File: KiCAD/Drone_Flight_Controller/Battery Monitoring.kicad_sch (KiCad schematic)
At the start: 7 parts, among them U2 AS358

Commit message: Add Components to BOM
Add Components to BOM
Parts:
- added unit 1 of U2
- R11, R15: footprint (none) -> Resistor_SMD:R_0805_2012Metric_Pad1.20x1.40mm_HandSolder; Link (none) -> https://www.mouser.at/ProductDetail/Panasonic/ERA-6AEB823V?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
- R12, R16: footprint (none) -> Resistor_SMD:R_0805_2012Metric_Pad1.20x1.40mm_HandSolder; Link (none) -> https://www.mouser.at/ProductDetail/Panasonic/ERA-6AEB272V?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
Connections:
- net BATT Monitor: now also U2.1; no longer U2.1
- net at R14.2, R15.1: now also U2.2 (-); no longer U2.2 (-)
- net at R12.2, R13.1: now also U2.3 (+); no longer U2.3 (+)
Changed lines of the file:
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@@
 			)
 		)
-		(property "Footprint" ""
+		(property "Footprint" "Resistor_SMD:R_0805_2012Metric_Pad1.20x1.40mm_HandSolder"
 			(at 90.17 52.578 90)
 			(effects
@@
 			)
 		)
-		(property "Datasheet" "~"
+		(property "Datasheet" "https://industrial.panasonic.com/cdbs/www-data/pdf/RDM0000/AOA0000C307.pdf"
 			(at 90.17 50.8 0)
 			(effects
@@
 		(property "Description" "Resistor"
 			(at 90.17 50.8 0)
+			(effects
+				(font
+					(size 1.27 1.27)
+				)
+				(hide yes)
+			)
+		)
+		(property "Link" "https://www.mouser.at/ProductDetail/Panasonic/ERA-6AEB823V?qs=sGAEpiMZZMtlubZbdhIBINMa8yaPrN5wJK7%252Bt6nJOdc%3D"
+			(at 90.17 50.8 90)
 			(effects
 				(font
@@
 			)
 		)
-		(property "Footprint" ""
+		(property "Footprint" "Resistor_SMD:R_0805_2012Metric_Pad1.20x1.40mm_HandSolder"
 			(at 100.33 52.578 90)
 			(effects
@@
 			)
 		)
-		(property "Datasheet" "~"
+		(property "Datasheet" "https://industrial.panasonic.com/cdbs/www-data/pdf/RDM0000/AOA0000C307.pdf"
 			(at 100.33 50.8 0)
 			(effects
@@
 		(property "Description" "Resistor"
 			(at 100.33 50.8 0)
+			(effects
+				(font
+					(size 1.27 1.27)
+				)
+				(hide yes)
+			)
+		)
+		(property "Link" "https://www.mouser.at/ProductDetail/Panasonic/ERA-6AEB272V?qs=sGAEpiMZZMtlubZbdhIBINMa8yaPrN5wOlaFrC8qQgQ%3D"
+			(at 100.33 50.8 90)
 			(effects
 				(font
@@
 			)
 		)
-		(property "Footprint" ""
+		(property "Footprint" "Resistor_SMD:R_0805_2012Metric_Pad1.20x1.40mm_HandSolder"
 			(at 68.58 41.148 90)
 			(effects
@@
 			)
 		)
-		(property "Datasheet" "~"
+		(property "Datasheet" "https://industrial.panasonic.com/cdbs/www-data/pdf/RDM0000/AOA0000C307.pdf"
 			(at 68.58 39.37 0)
 			(effects
@@
 		(property "Description" "Resistor"
 			(at 68.58 39.37 0)
+			(effects
+				(font
+					(size 1.27 1.27)
+				)
+				(hide yes)
+			)
+		)
+		(property "Link" "https://www.mouser.at/ProductDetail/Panasonic/ERA-6AEB823V?qs=sGAEpiMZZMtlubZbdhIBINMa8yaPrN5wJK7%252Bt6nJOdc%3D"
+			(at 68.58 39.37 90)
 			(effects
 				(font
@@
 			)
 		)
-		(property "Footprint" ""
+		(property "Footprint" "Resistor_SMD:R_0805_2012Metric_Pad1.20x1.40mm_HandSolder"
 			(at 78.74 41.148 90)
 			(effects
@@
 			)
 		)
-		(property "Datasheet" "~"
+		(property "Datasheet" "https://industrial.panasonic.com/cdbs/www-data/pdf/RDM0000/AOA0000C307.pdf"
 			(at 78.74 39.37 0)
 			(effects
@@
 			(effects
 				(font
+					(size 1.27 1.27)
+				)
+				(hide yes)
+			)
+		)
+		(property "Link" "https://www.mouser.at/ProductDetail/Panasonic/ERA-6AEB272V?qs=sGAEpiMZZMtlubZbdhIBINMa8yaPrN5wOlaFrC8qQgQ%3D"
+			(at 78.74 39.37 90)
+			(effects
+				(font

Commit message: Reanotate
Reanotate
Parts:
- renumbered R11 to R601, R12 to R602, R14 to R603, R15 to R604, R13 to R605, R16 to R606, U2 to U301
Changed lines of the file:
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@@
 		(on_board yes)
 		(dnp no)
-		(property "Reference" "R15"
+		(property "Reference" "R604"
 			(at 90.17 53.34 90)
 			(effects
@@
 			(project "Drone_Flight_Controller"
 				(path "/05daaa24-e506-4b9a-9564-8bf799413ca8/8aeacdae-c3f2-480a-a34d-37642627b117"
-					(reference "R15")
+					(reference "R604")
 					(unit 1)
 				)
@@
 		(on_board yes)
 		(dnp no)
-		(property "Reference" "R16"
+		(property "Reference" "R606"
 			(at 100.33 53.34 90)
 			(effects
@@
 			(project "Drone_Flight_Controller"
 				(path "/05daaa24-e506-4b9a-9564-8bf799413ca8/8aeacdae-c3f2-480a-a34d-37642627b117"
-					(reference "R16")
+					(reference "R606")
 					(unit 1)
 				)
@@
 		(dnp no)
 		(fields_autoplaced yes)
-		(property "Reference" "R13"
+		(property "Reference" "R605"
 			(at 95.25 21.59 90)
 			(effects
@@
 			(project ""
 				(path "/05daaa24-e506-4b9a-9564-8bf799413ca8/8aeacdae-c3f2-480a-a34d-37642627b117"
-					(reference "R13")
+					(reference "R605")
 					(unit 1)
 				)
@@
 		(dnp no)
 		(fields_autoplaced yes)
-		(property "Reference" "U2"
+		(property "Reference" "U301"
 			(at 115.57 58.42 0)
 			(effects
@@
 			(project "Drone_Flight_Controller"
 				(path "/05daaa24-e506-4b9a-9564-8bf799413ca8/8aeacdae-c3f2-480a-a34d-37642627b117"
-					(reference "U2")
+					(reference "U301")
 					(unit 2)
 				)
@@
 		(dnp no)
 		(fields_autoplaced yes)
-		(property "Reference" "U2"
+		(property "Reference" "U301"
 			(at 95.25 31.75 0)
 			(effects
@@
 			(project "Drone_Flight_Controller"
 				(path "/05daaa24-e506-4b9a-9564-8bf799413ca8/8aeacdae-c3f2-480a-a34d-37642627b117"
-					(reference "U2")
+					(reference "U301")
 					(unit 1)
 				)
@@
 		(on_board yes)
 		(dnp no)
-		(property "Reference" "R14"
+		(property "Reference" "R603"
 			(at 78.74 47.244 90)
 			(effects
@@
 			(project "Drone_Flight_Controller"
 				(path "/05daaa24-e506-4b9a-9564-8bf799413ca8/8aeacdae-c3f2-480a-a34d-37642627b117"
-					(reference "R14")
+					(reference "R603")
 					(unit 1)
 				)
@@
 		(dnp no)
 		(fields_autoplaced yes)
-		(property "Reference" "#PWR015"
+		(property "Reference" "#PWR0601"
 			(at 40.64 36.83 0)
 			(effects
@@
 			(project ""
 				(path "/05daaa24-e506-4b9a-9564-8bf799413ca8/8aeacdae-c3f2-480a-a34d-37642627b117"
-					(reference "#PWR015")
+					(reference "#PWR0601")
 					(unit 1)
 				)
@@
 		(dnp no)
 		(fields_autoplaced yes)
-		(property "Reference" "#PWR014"
+		(property "Reference" "#PWR0602"
 			(at 50.8 36.83 0)
 			(effects
@@
 			(project ""
 				(path "/05daaa24-e506-4b9a-9564-8bf799413ca8/8aeacdae-c3f2-480a-a34d-37642627b117"
-					(reference "#PWR014")
+					(reference "#PWR0602")
 					(unit 1)
 				)
@@
 		(dnp no)
 		(fields_autoplaced yes)
-		(property "Reference" "#PWR018"
+		(property "Reference" "#PWR0603"
 			(at 104.14 71.12 0)
 			(effects
@@
 			(project ""
 				(path "/05daaa24-e506-4b9a-9564-8bf799413ca8/8aeacdae-c3f2-480a-a34d-37642627b117"
-					(reference "#PWR018")
+					(reference "#PWR0603")
 					(unit 1)
 				)
@@
 		(dnp no)
 		(fields_autoplaced yes)
-		(property "Reference" "#PWR016"
+		(property "Reference" "#PWR0604"
 			(at 105.41 26.67 0)
 			(effects
@@
 			(project ""
 				(path "/05daaa24-e506-4b9a-9564-8bf799413ca8/8aeacdae-c3f2-480a-a34d-37642627b117"
-					(reference "#PWR016")
+					(reference "#PWR0604")
 					(unit 1)
 				)
@@
 		(dnp no)
 		(fields_autoplaced yes)
-		(property "Reference" "R11"
+		(property "Reference" "R601"
 			(at 68.58 33.02 90)
 			(effects
@@
 			(project ""
 				(path "/05daaa24-e506-4b9a-9564-8bf799413ca8/8aeacdae-c3f2-480a-a34d-37642627b117"
-					(reference "R11")
+					(reference "R601")
 					(unit 1)
 				)
@@
 		(dnp no)
 		(fields_autoplaced yes)
-		(property "Reference" "R12"
+		(property "Reference" "R602"
 			(at 78.74 33.02 90)
 			(effects
@@
 			(project "Drone_Flight_Controller"
 				(path "/05daaa24-e506-4b9a-9564-8bf799413ca8/8aeacdae-c3f2-480a-a34d-37642627b117"
-					(reference "R12")
-					(unit 1)
-				)
+					(reference "R602")
+					(unit 1)
+				)

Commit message: Reannotate
Reannotate
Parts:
- renumbered R605 to R601, R601 to R602, R602 to R603, R603 to R604, R604 to R605, U301 to U302
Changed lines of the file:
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@@
 		(on_board yes)
 		(dnp no)
-		(property "Reference" "R604"
+		(property "Reference" "R605"
 			(at 90.17 53.34 90)
 			(effects
@@
 			(project "Drone_Flight_Controller"
 				(path "/05daaa24-e506-4b9a-9564-8bf799413ca8/8aeacdae-c3f2-480a-a34d-37642627b117"
-					(reference "R604")
+					(reference "R605")
 					(unit 1)
 				)
@@
 		(dnp no)
 		(fields_autoplaced yes)
-		(property "Reference" "R605"
+		(property "Reference" "R601"
 			(at 95.25 21.59 90)
 			(effects
@@
 			(project ""
 				(path "/05daaa24-e506-4b9a-9564-8bf799413ca8/8aeacdae-c3f2-480a-a34d-37642627b117"
-					(reference "R605")
+					(reference "R601")
 					(unit 1)
 				)
@@
 		(dnp no)
 		(fields_autoplaced yes)
-		(property "Reference" "U301"
+		(property "Reference" "U302"
 			(at 115.57 58.42 0)
 			(effects
@@
 			(project "Drone_Flight_Controller"
 				(path "/05daaa24-e506-4b9a-9564-8bf799413ca8/8aeacdae-c3f2-480a-a34d-37642627b117"
-					(reference "U301")
+					(reference "U302")
 					(unit 2)
 				)
@@
 		(dnp no)
 		(fields_autoplaced yes)
-		(property "Reference" "U301"
+		(property "Reference" "U302"
 			(at 95.25 31.75 0)
 			(effects
@@
 			(project "Drone_Flight_Controller"
 				(path "/05daaa24-e506-4b9a-9564-8bf799413ca8/8aeacdae-c3f2-480a-a34d-37642627b117"
-					(reference "U301")
+					(reference "U302")
 					(unit 1)
 				)
@@
 		(on_board yes)
 		(dnp no)
-		(property "Reference" "R603"
+		(property "Reference" "R604"
 			(at 78.74 47.244 90)
 			(effects
@@
 			(project "Drone_Flight_Controller"
 				(path "/05daaa24-e506-4b9a-9564-8bf799413ca8/8aeacdae-c3f2-480a-a34d-37642627b117"
-					(reference "R603")
+					(reference "R604")
 					(unit 1)
 				)
@@
 		(dnp no)
 		(fields_autoplaced yes)
-		(property "Reference" "#PWR0601"
+		(property "Reference" "#PWR0602"
 			(at 40.64 36.83 0)
 			(effects
@@
 			(project ""
 				(path "/05daaa24-e506-4b9a-9564-8bf799413ca8/8aeacdae-c3f2-480a-a34d-37642627b117"
-					(reference "#PWR0601")
+					(reference "#PWR0602")
 					(unit 1)
 				)
@@
 		(dnp no)
 		(fields_autoplaced yes)
-		(property "Reference" "#PWR0602"
+		(property "Reference" "#PWR0603"
 			(at 50.8 36.83 0)
 			(effects
@@
 			(project ""
 				(path "/05daaa24-e506-4b9a-9564-8bf799413ca8/8aeacdae-c3f2-480a-a34d-37642627b117"
-					(reference "#PWR0602")
+					(reference "#PWR0603")
 					(unit 1)
 				)
@@
 		(dnp no)
 		(fields_autoplaced yes)
-		(property "Reference" "#PWR0603"
+		(property "Reference" "#PWR0604"
 			(at 104.14 71.12 0)
 			(effects
@@
 			(project ""
 				(path "/05daaa24-e506-4b9a-9564-8bf799413ca8/8aeacdae-c3f2-480a-a34d-37642627b117"
-					(reference "#PWR0603")
+					(reference "#PWR0604")
 					(unit 1)
 				)
@@
 		(dnp no)
 		(fields_autoplaced yes)
-		(property "Reference" "#PWR0604"
+		(property "Reference" "#PWR0601"
 			(at 105.41 26.67 0)
 			(effects
@@
 			(project ""
 				(path "/05daaa24-e506-4b9a-9564-8bf799413ca8/8aeacdae-c3f2-480a-a34d-37642627b117"
-					(reference "#PWR0604")
+					(reference "#PWR0601")
 					(unit 1)
 				)
@@
 		(dnp no)
 		(fields_autoplaced yes)
-		(property "Reference" "R601"
+		(property "Reference" "R602"
 			(at 68.58 33.02 90)
 			(effects
@@
 			(project ""
 				(path "/05daaa24-e506-4b9a-9564-8bf799413ca8/8aeacdae-c3f2-480a-a34d-37642627b117"
-					(reference "R601")
+					(reference "R602")
 					(unit 1)
 				)
@@
 		(dnp no)
 		(fields_autoplaced yes)
-		(property "Reference" "R602"
+		(property "Reference" "R603"
 			(at 78.74 33.02 90)
 			(effects
@@
 			(project "Drone_Flight_Controller"
 				(path "/05daaa24-e506-4b9a-9564-8bf799413ca8/8aeacdae-c3f2-480a-a34d-37642627b117"
-					(reference "R602")
-					(unit 1)
-				)
+					(reference "R603")
+					(unit 1)
+				)

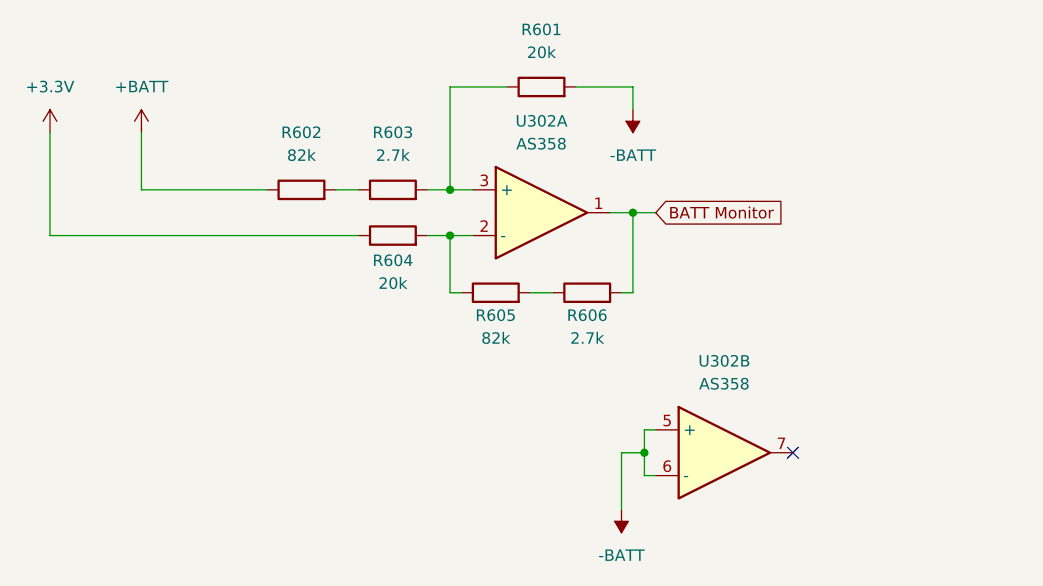
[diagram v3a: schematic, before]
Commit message: Add Unity gain Amp to Battery Monitor
Add Unity Gain Amp to Battery Monitor
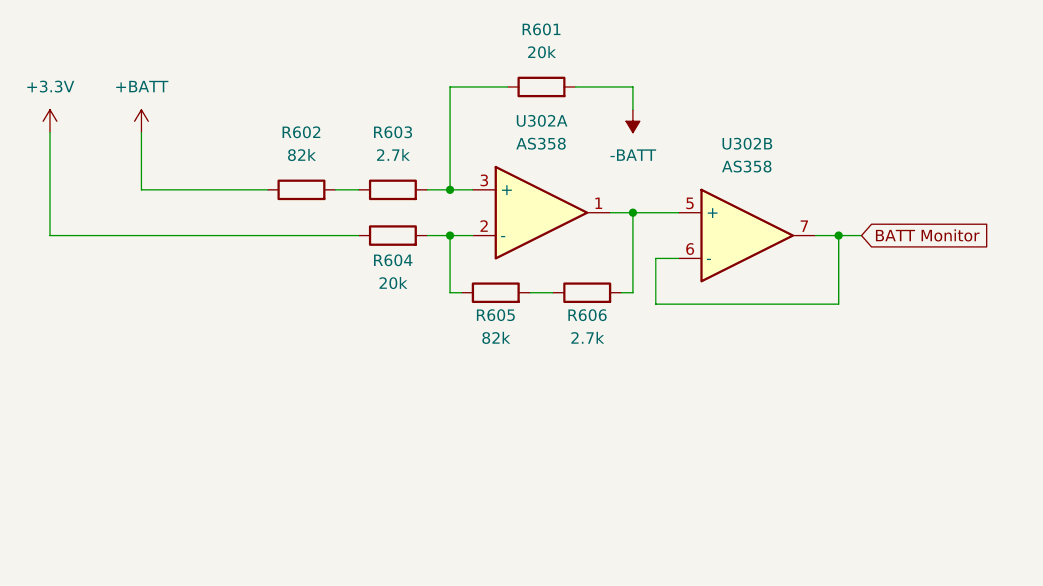
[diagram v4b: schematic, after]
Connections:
- net -BATT: no longer U302.5 (+), U302.6 (-)
- net BATT Monitor: now also U302.6 (-), U302.7; no longer R606.2, U302.1
- new net: R606.2, U302.1, U302.5 (+)
- no-connect marks 1 -> 0
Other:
- moved on the sheet: U302B
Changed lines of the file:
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@@
 	(title_block
 		(title "Battery Monitoring")
-		(date "2025-07-07")
+		(date "2025-07-18")
 		(rev "V1")
 		(company "HTL Steyr")
 		(comment 1 "Brandner")
-	)
-	(junction
-		(at 106.68 68.58)
-		(diameter 0)
-		(color 0 0 0 0)
 	)
 	(junction
@@
 	)
 	(junction
+		(at 128.27 44.45)
+		(diameter 0)
+		(color 0 0 0 0)
+	)
+	(junction
 		(at 105.41 41.91)
 		(diameter 0)
 		(color 0 0 0 0)
 	)
-	(no_connect
-		(at 123.19 68.58)
-	)
-	(wire
-		(pts
-			(xy 105.41 41.91) (xy 107.95 41.91)
+	(wire
+		(pts
+			(xy 105.41 41.91) (xy 110.49 41.91)
 		)
 		(stroke
@@
 	(wire
 		(pts
+			(xy 128.27 44.45) (xy 130.81 44.45)
+		)
+		(stroke
+			(width 0)
+			(type default)
+		)
+	)
+	(wire
+		(pts
+			(xy 107.95 46.99) (xy 107.95 52.07)
+		)
+		(stroke
+			(width 0)
+			(type default)
+		)
+	)
+	(wire
+		(pts
 			(xy 85.09 50.8) (xy 85.09 44.45)
 		)
@@
 	(wire
 		(pts
-			(xy 106.68 71.12) (xy 107.95 71.12)
+			(xy 128.27 52.07) (xy 128.27 44.45)
+		)
+		(stroke
+			(width 0)
+			(type default)
+		)
+	)
+	(wire
+		(pts
+			(xy 110.49 46.99) (xy 107.95 46.99)
 		)
 		(stroke
@@
 	(wire
 		(pts
-			(xy 106.68 66.04) (xy 106.68 68.58)
-		)
-		(stroke
-			(width 0)
-			(type default)
-		)
-	)
-	(wire
-		(pts
-			(xy 106.68 68.58) (xy 106.68 71.12)
+			(xy 125.73 44.45) (xy 128.27 44.45)
 		)
 		(stroke
@@
 	(wire
 		(pts
-			(xy 104.14 74.93) (xy 104.14 68.58)
-		)
-		(stroke
-			(width 0)
-			(type default)
-		)
-	)
-	(wire
-		(pts
 			(xy 93.98 50.8) (xy 96.52 50.8)
 		)
@@
 	(wire
 		(pts
+			(xy 107.95 52.07) (xy 128.27 52.07)
+		)
+		(stroke
+			(width 0)
+			(type default)
+		)
+	)
+	(wire
+		(pts
 			(xy 102.87 41.91) (xy 105.41 41.91)
 		)
@@
 		(pts
 			(xy 85.09 27.94) (xy 85.09 39.37)
-		)
-		(stroke
-			(width 0)
-			(type default)
-		)
-	)
-	(wire
-		(pts
-			(xy 104.14 68.58) (xy 106.68 68.58)
-		)
-		(stroke
-			(width 0)
-			(type default)
-		)
-	)
-	(wire
-		(pts
-			(xy 107.95 66.04) (xy 106.68 66.04)
 		)
 		(stroke
@@
 	(global_label "BATT Monitor"
 		(shape input)
-		(at 107.95 41.91 0)
+		(at 130.81 44.45 0)
 		(fields_autoplaced yes)
 		(effects
@@
 		)
 		(property "Intersheetrefs" "${INTERSHEET_REFS}"
-			(at 123.2117 41.91 0)
+			(at 146.0717 44.45 0)
 			(effects
 				(font
@@
 	(symbol
 		(lib_id "Device:Opamp_Dual")
-		(at 115.57 68.58 0)
+		(at 118.11 44.45 0)
 		(unit 2)
 		(exclude_from_sim no)
@@
 		(fields_autoplaced yes)
 		(property "Reference" "U302"
-			(at 115.57 58.42 0)
+			(at 118.11 34.29 0)
 			(effects
 				(font
@@
 		)
 		(property "Value" "AS358"
-			(at 115.57 60.96 0)
+			(at 118.11 36.83 0)
 			(effects
 				(font
@@
 		)
 		(property "Footprint" "Package_SO:SO-8_3.9x4.9mm_P1.27mm"
-			(at 115.57 68.58 0)
+			(at 118.11 44.45 0)
 			(effects
 				(font
@@
 		)
 		(property "Datasheet" "https://www.mouser.at/datasheet/2/115/DIOD_S_A0005046231_1-2542568.pdf"
-			(at 115.57 68.58 0)
+			(at 118.11 44.45 0)
 			(effects
 				(font
@@
 		)
 		(property "Description" "Dual operational amplifier"
-			(at 115.57 68.58 0)
+			(at 118.11 44.45 0)
 			(effects
 				(font
@@
 		)
 		(property "Sim.Library" "${KICAD9_SYMBOL_DIR}/Simulation_SPICE.sp"
-			(at 115.57 68.58 0)
+			(at 118.11 44.45 0)
 			(effects
 				(font
@@
 		)
 		(property "Sim.Name" "kicad_builtin_opamp_dual"
-			(at 115.57 68.58 0)
+			(at 118.11 44.45 0)
 			(effects
 				(font
@@
 		)
 		(property "Sim.Device" "SUBCKT"
-			(at 115.57 68.58 0)
+			(at 118.11 44.45 0)
 			(effects
 				(font
@@
 		)
 		(property "Sim.Pins" "1=out1 2=in1- 3=in1+ 4=vee 5=in2+ 6=in2- 7=out2 8=vcc"
-			(at 115.57 68.58 0)
+			(at 118.11 44.45 0)
 			(effects
 				(font
@@
 		)
 		(property "Link" "https://www.mouser.at/ProductDetail/Diodes-Incorporated/AS358MTR-G1?qs=FKu9oBikfSlRUA%252BzgDv25w%3D%3D"
-			(at 115.57 68.58 0)
+			(at 118.11 44.45 0)
 			(effects
 				(font
@@
 					(unit 1)
 				)
-			)
-		)
-	)
-	(symbol
-		(lib_id "power:-BATT")
-		(at 104.14 74.93 180)
-		(unit 1)
-		(exclude_from_sim no)
-		(in_bom yes)
-		(on_board yes)
-		(dnp no)
-		(fields_autoplaced yes)
-		(property "Reference" "#PWR0604"
-			(at 104.14 71.12 0)
-			(effects
-				(font
-					(size 1.27 1.27)
-				)
-				(hide yes)
-			)
-		)
-		(property "Value" "-BATT"
-			(at 104.14 80.01 0)
-			(effects
-				(font
-					(size 1.27 1.27)
-				)
-			)
-		)
-		(property "Footprint" ""
-			(at 104.14 74.93 0)
-			(effects
-				(font
-					(size 1.27 1.27)
-				)
-				(hide yes)
-			)
-		)
-		(property "Datasheet" ""
-			(at 104.14 74.93 0)
-			(effects
-				(font
-					(size 1.27 1.27)
-				)
-				(hide yes)
-			)
-		)
-		(property "Description" "Power symbol creates a global label with name \"-BATT\""
-			(at 104.14 74.93 0)
-			(effects
-				(font
-					(size 1.27 1.27)
-				)
-				(hide yes)
-			)
-		)
-		(pin "1"
-		)
-		(instances
-			(project ""
-				(path "/05daaa24-e506-4b9a-9564-8bf799413ca8/8aeacdae-c3f2-480a-a34d-37642627b117"
-					(reference "#PWR0604")
-					(unit 1)
-				)

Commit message: Reannotate
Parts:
- renumbered R601 to R501, R602 to R502, R603 to R503, R604 to R504, R605 to R505, R606 to R506, U302 to U205
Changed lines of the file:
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@@
 		(on_board yes)
 		(dnp no)
-		(property "Reference" "R605"
+		(property "Reference" "R505"
 			(at 90.17 53.34 90)
 			(effects
@@
 			(project "Drone_Flight_Controller"
 				(path "/05daaa24-e506-4b9a-9564-8bf799413ca8/8aeacdae-c3f2-480a-a34d-37642627b117"
-					(reference "R605")
+					(reference "R505")
 					(unit 1)
 				)
@@
 		(on_board yes)
 		(dnp no)
-		(property "Reference" "R606"
+		(property "Reference" "R506"
 			(at 100.33 53.34 90)
 			(effects
@@
 			(project "Drone_Flight_Controller"
 				(path "/05daaa24-e506-4b9a-9564-8bf799413ca8/8aeacdae-c3f2-480a-a34d-37642627b117"
-					(reference "R606")
+					(reference "R506")
 					(unit 1)
 				)
@@
 		(dnp no)
 		(fields_autoplaced yes)
-		(property "Reference" "R601"
+		(property "Reference" "R501"
 			(at 95.25 21.59 90)
 			(effects
@@
 			(project ""
 				(path "/05daaa24-e506-4b9a-9564-8bf799413ca8/8aeacdae-c3f2-480a-a34d-37642627b117"
-					(reference "R601")
+					(reference "R501")
 					(unit 1)
 				)
@@
 		(dnp no)
 		(fields_autoplaced yes)
-		(property "Reference" "U302"
+		(property "Reference" "U205"
 			(at 118.11 34.29 0)
 			(effects
@@
 			(project "Drone_Flight_Controller"
 				(path "/05daaa24-e506-4b9a-9564-8bf799413ca8/8aeacdae-c3f2-480a-a34d-37642627b117"
-					(reference "U302")
+					(reference "U205")
 					(unit 2)
 				)
@@
 		(dnp no)
 		(fields_autoplaced yes)
-		(property "Reference" "U302"
+		(property "Reference" "U205"
 			(at 95.25 31.75 0)
 			(effects
@@
 			(project "Drone_Flight_Controller"
 				(path "/05daaa24-e506-4b9a-9564-8bf799413ca8/8aeacdae-c3f2-480a-a34d-37642627b117"
-					(reference "U302")
+					(reference "U205")
 					(unit 1)
 				)
@@
 		(on_board yes)
 		(dnp no)
-		(property "Reference" "R604"
+		(property "Reference" "R504"
 			(at 78.74 47.244 90)
 			(effects
@@
 			(project "Drone_Flight_Controller"
 				(path "/05daaa24-e506-4b9a-9564-8bf799413ca8/8aeacdae-c3f2-480a-a34d-37642627b117"
-					(reference "R604")
+					(reference "R504")
 					(unit 1)
 				)
@@
 		(dnp no)
 		(fields_autoplaced yes)
-		(property "Reference" "#PWR0602"
+		(property "Reference" "#PWR0502"
 			(at 40.64 36.83 0)
 			(effects
@@
 			(project ""
 				(path "/05daaa24-e506-4b9a-9564-8bf799413ca8/8aeacdae-c3f2-480a-a34d-37642627b117"
-					(reference "#PWR0602")
+					(reference "#PWR0502")
 					(unit 1)
 				)
@@
 		(dnp no)
 		(fields_autoplaced yes)
-		(property "Reference" "#PWR0603"
+		(property "Reference" "#PWR0503"
 			(at 50.8 36.83 0)
 			(effects
@@
 			(project ""
 				(path "/05daaa24-e506-4b9a-9564-8bf799413ca8/8aeacdae-c3f2-480a-a34d-37642627b117"
-					(reference "#PWR0603")
+					(reference "#PWR0503")
 					(unit 1)
 				)
@@
 		(dnp no)
 		(fields_autoplaced yes)
-		(property "Reference" "#PWR0601"
+		(property "Reference" "#PWR0501"
 			(at 105.41 26.67 0)
 			(effects
@@
 			(project ""
 				(path "/05daaa24-e506-4b9a-9564-8bf799413ca8/8aeacdae-c3f2-480a-a34d-37642627b117"
-					(reference "#PWR0601")
+					(reference "#PWR0501")
 					(unit 1)
 				)
@@
 		(dnp no)
 		(fields_autoplaced yes)
-		(property "Reference" "R602"
+		(property "Reference" "R502"
 			(at 68.58 33.02 90)
 			(effects
@@
 			(project ""
 				(path "/05daaa24-e506-4b9a-9564-8bf799413ca8/8aeacdae-c3f2-480a-a34d-37642627b117"
-					(reference "R602")
+					(reference "R502")
 					(unit 1)
 				)
@@
 		(dnp no)
 		(fields_autoplaced yes)
-		(property "Reference" "R603"
+		(property "Reference" "R503"
 			(at 78.74 33.02 90)
 			(effects
@@
 			(project "Drone_Flight_Controller"
 				(path "/05daaa24-e506-4b9a-9564-8bf799413ca8/8aeacdae-c3f2-480a-a34d-37642627b117"
-					(reference "R603")
-					(unit 1)
-				)
+					(reference "R503")
+					(unit 1)
+				)
